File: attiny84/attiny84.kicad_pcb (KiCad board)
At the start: 2 copper layers, 159.9 x 99.9 mm, 58 parts, among them J1 DIN41612_02x16_AB, J2 USB_C_Receptacle_USB2.0, J3 Screw_Terminal_01x03, J4 Screw_Terminal_01x03, J5 Screw_Terminal_01x03, J6 Screw_Terminal_01x03, Q1 BSS138, Q2 BSS138, Q3 BT138-800, Q4 DMG2305UX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

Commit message: Removed reset pin on backplane
The connection between the reset pin and the backplane has been removed
as it is not required. The reset pin on the backplane served no function
as it would be near impossible to use in practice and was likely to
cause issues surrounding pullup resistors if too many boards were added.
As such, the link between the backplane and the IC reset pins has been
removed, leaving only the reset button on the board.

Fixes #1

Signed-off-by: Matthew Nickson <mnickson@sidingsmedia.com>
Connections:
- J1 pad b10: /~{RESET} -> unconnected-(J1-Padb10)
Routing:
- net /~{RESET}: track 157.6 -> 47.2 mm
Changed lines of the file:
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@@
   (paper "A4")
   (title_block
-    (title "Speed Controller")
-    (date "2022-11-26")
-    (rev "0.3")
+    (title "Speed Control Node")
+    (date "2022-12-20")
+    (rev "0.4")
     (company "Sidings Media")
     (comment 1 "Licence: CERN-OHL-P-2.0 or any later version")
@@
   (net 73 "unconnected-(U3-Pad6)")
   (net 74 "/Motor Driver/IN1")
+  (net 75 "unconnected-(J1-Padb10)")
   (footprint "Mounting_Holes:MountingHole_2.7mm" locked (layer "F.Cu")
     (at 58.6 139.45)
@@
       (net 6 "GND") (pinfunction "Pin_b9") (pintype "passive"))
     (pad "b10" thru_hole circle (at 22.86 2.54 90) (size 1.55 1.55) (drill 1) (layers *.Cu *.Mask)
-      (net 7 "/~{RESET}") (pinfunction "Pin_b10") (pintype "passive"))
+      (net 75 "unconnected-(J1-Padb10)") (pinfunction "Pin_b10") (pintype "passive+no_connect"))
     (pad "b11" thru_hole circle (at 25.4 2.54 90) (size 1.55 1.55) (drill 1) (layers *.Cu *.Mask)
       (net 38 "unconnected-(J1-Padb11)") (pinfunction "Pin_b11") (pintype "passive+no_connect"))
@@
   (via (at 72.68 141.53) (size 0.8) (drill 0.4) (layers "F.Cu" "B.Cu") (free) (net 6))
   (via (at 192.68 141.53) (size 0.8) (drill 0.4) (layers "F.Cu" "B.Cu") (free) (net 6))
-  (segment (start 165.765 91.195) (end 171.13 85.83) (width 0.25) (layer "F.Cu") (net 7))
   (segment (start 171.28 82.7925) (end 171.1425 82.93) (width 0.25) (layer "F.Cu") (net 7))
   (segment (start 196.005 63.03) (end 196.381751 63.03) (width 0.25) (layer "F.Cu") (net 7))
@@
   (segment (start 173.88 73.93) (end 175.18 72.63) (width 0.25) (layer "F.Cu") (net 7))
   (segment (start 175.78 67.73) (end 175.18 68.33) (width 0.25) (layer "F.Cu") (net 7))
-  (segment (start 62.925 91.195) (end 165.765 91.195) (width 0.25) (layer "F.Cu") (net 7))
   (segment (start 172.38 77.33) (end 171.28 78.43) (width 0.25) (layer "F.Cu") (net 7))
   (segment (start 197.78 66.83) (end 196.88 67.73) (width 0.25) (layer "F.Cu") (net 7))
@@
   )
   (zone (net 6) (net_name "GND") (layers F&B.Cu) (hatch edge 0.508)
-    (connect_pads yes (clearance 0))
+    (connect_pads (clearance 0))
     (min_thickness 0.254) (filled_areas_thickness no)
     (fill yes (thermal_gap 0.508) (thermal_bridge_width 0.508) (smoothing fillet) (radius 1))

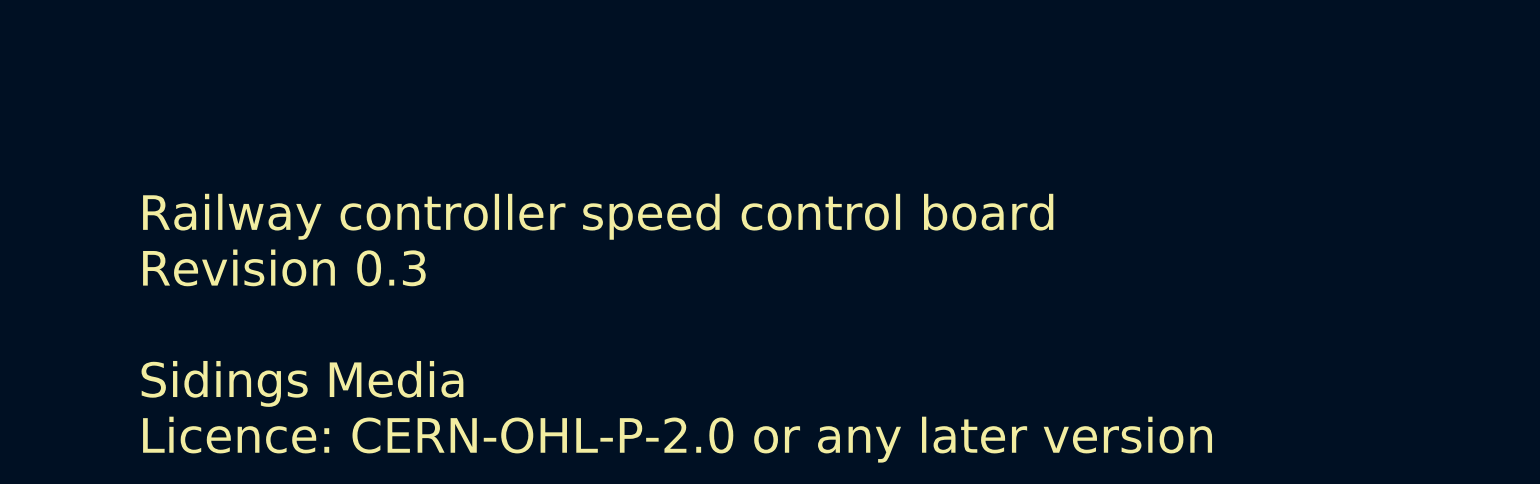
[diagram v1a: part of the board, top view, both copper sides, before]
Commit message: Fixed revision + terminology on silk screen
Signed-off-by: Matthew Nickson <mnickson@sidingsmedia.com>
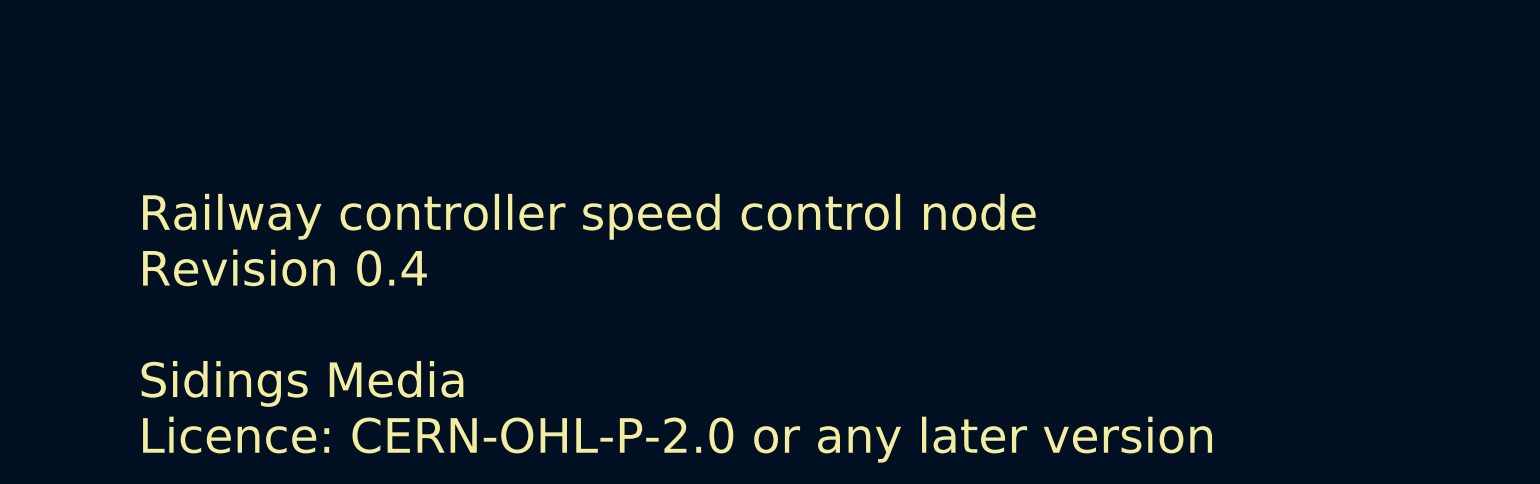
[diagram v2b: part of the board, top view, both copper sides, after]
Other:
- board text added: "Railway controller speed control node Revision 0.4 Sidings Media Licence: CERN-OHL-P-2.0 or any later version"
- board text removed: "Railway controller speed control board Revision 0.3 Sidings Media Licence: CERN-OHL-P-2.0 or any later version"
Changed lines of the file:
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@@
   (gr_line locked (start 55.1 142.5) (end 214.9 142.5) (layer "F.CrtYd") (width 0.2))
   (gr_line locked (start 214.9 47.5) (end 55.1 47.5) (layer "F.CrtYd") (width 0.2))
-  (gr_text "Railway controller speed control board\nRevision 0.3\n\nSidings Media\nLicence: CERN-OHL-P-2.0 or any later version" (at 68.68 133.43) (layer "F.SilkS")
+  (gr_text "Railway controller speed control node\nRevision 0.4\n\nSidings Media\nLicence: CERN-OHL-P-2.0 or any later version" (at 68.68 133.43) (layer "F.SilkS")
     (effects (font (size 1.5 1.5) (thickness 0.15)) (justify left))
   )
